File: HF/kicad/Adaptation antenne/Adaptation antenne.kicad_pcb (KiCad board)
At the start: 2 copper layers, 40.8 x 23.7 mm, 6 parts, among them J1 Conn_Coaxial, J2 Impédence Antenne, J3 impédence GND, J4 Sortie vers antenne, J5 Sortie vers GND, J6 Antenne

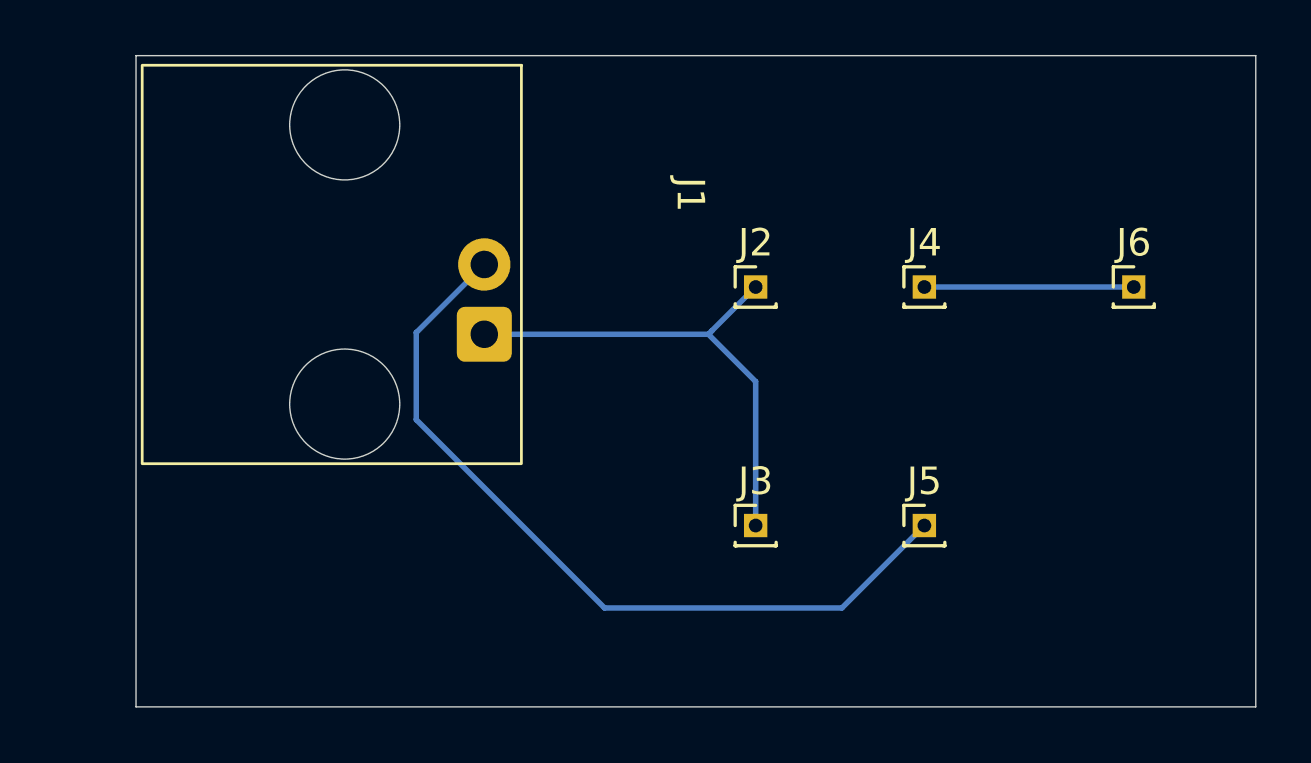
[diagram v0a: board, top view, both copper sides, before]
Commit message: modif kicad pour ajusté au test sur platin
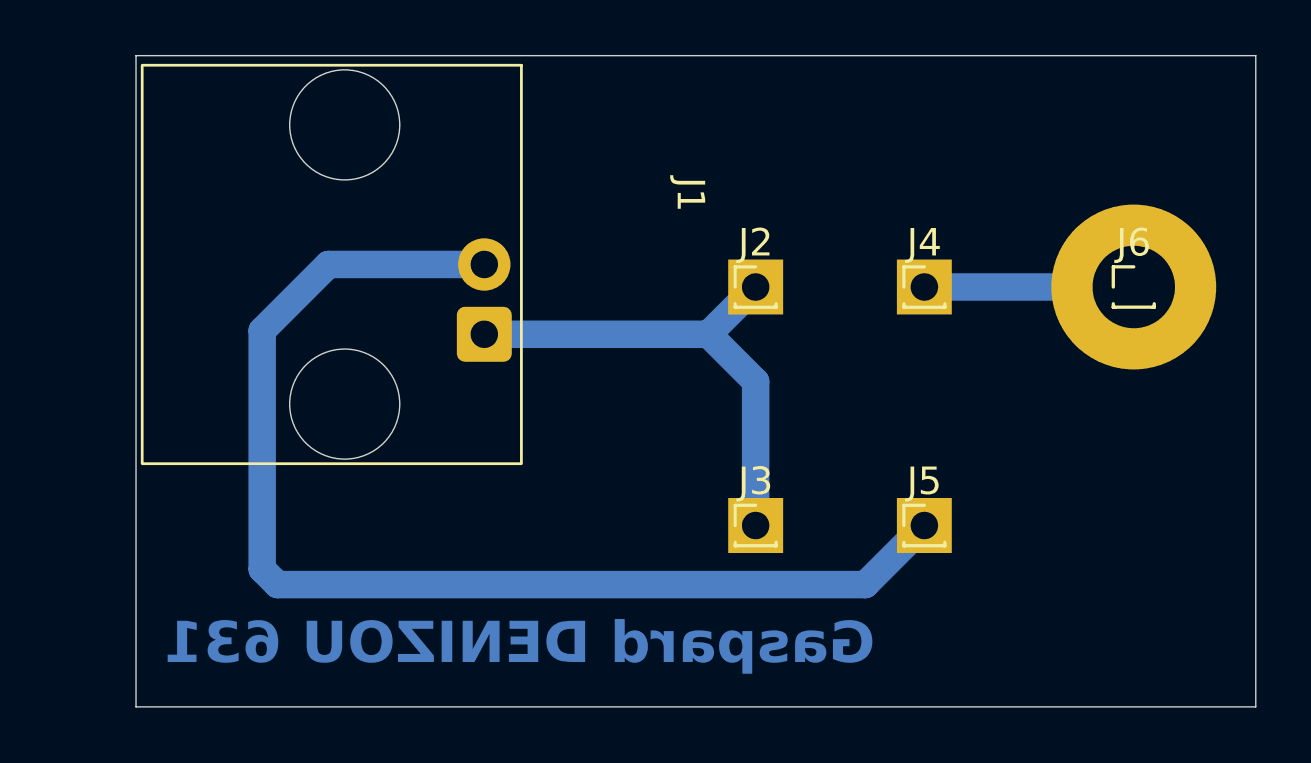
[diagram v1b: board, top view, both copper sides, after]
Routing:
- net GND: track 29.2 -> 43.0 mm
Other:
- board text added: "Gaspard DENIZOU 631"
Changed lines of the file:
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@@
 		(tenting front back)
 		(pcbplotparams
-			(layerselection 0x00000000_00000000_55555555_5755f5ff)
+			(layerselection 0x00000000_00000000_55555555_57555555)
 			(plot_on_all_layers_selection 0x00000000_00000000_00000000_00000000)
 			(disableapertmacros no)
@@
 			(outputformat 1)
 			(mirror no)
-			(drillshape 1)
+			(drillshape 0)
 			(scaleselection 1)
 			(outputdirectory "")
@@
 		(pad "1" thru_hole rect
 			(at 0 0)
-			(size 0.85 0.85)
-			(drill 0.5)
+			(size 2 2)
+			(drill 1)
 			(layers "*.Cu" "*.Mask")
 			(remove_unused_layers no)
@@
 		(pad "1" thru_hole rect
 			(at 0 0)
-			(size 0.85 0.85)
-			(drill 0.5)
+			(size 2 2)
+			(drill 1)
 			(layers "*.Cu" "*.Mask")
 			(remove_unused_layers no)
@@
 		(pad "1" thru_hole rect
 			(at 0 0)
-			(size 0.85 0.85)
-			(drill 0.5)
+			(size 2 2)
+			(drill 1)
 			(layers "*.Cu" "*.Mask")
 			(remove_unused_layers no)
@@
 			)
 		)
-		(pad "1" thru_hole rect
+		(pad "1" thru_hole circle
 			(at 0 0)
-			(size 0.85 0.85)
-			(drill 0.5)
+			(size 6 6)
+			(drill 3)
 			(layers "*.Cu" "*.Mask")
 			(remove_unused_layers no)
@@
 		(pad "1" thru_hole rect
 			(at 0 0)
-			(size 0.85 0.85)
-			(drill 0.5)
+			(size 2 2)
+			(drill 1)
 			(layers "*.Cu" "*.Mask")
 			(remove_unused_layers no)
@@
 		(layer "F.Fab")
 	)
+	(gr_text "Gaspard DENIZOU 631"
+		(at 38.85 34.15 0)
+		(layer "B.Cu")
+		(effects
+			(font
+				(size 1.5 1.5)
+				(thickness 0.3)
+				(bold yes)
+			)
+			(justify left bottom mirror)
+		)
+	)
 	(segment
 		(start 34.5 23.76)
 		(end 32.78 22.04)
-		(width 0.2)
+		(width 1)
 		(layer "B.Cu")
 		(net 1)
@@
 		(start 34.5 29)
 		(end 34.5 23.76)
-		(width 0.2)
+		(width 1)
 		(layer "B.Cu")
 		(net 1)
@@
 		(start 32.78 22.04)
 		(end 32.91 21.91)
-		(width 0.2)
+		(width 1)
 		(layer "B.Cu")
 		(net 1)
@@
 		(start 32.91 21.91)
 		(end 34.5 20.32)
-		(width 0.2)
+		(width 1)
 		(layer "B.Cu")
 		(net 1)
@@
 		(start 24.625 22.04)
 		(end 32.78 22.04)
-		(width 0.2)
+		(width 1)
 		(layer "B.Cu")
 		(net 1)
 	)
 	(segment
-		(start 29 32)
-		(end 37.64 32)
-		(width 0.2)
+		(start 16.541502 30.591502)
+		(end 16.541502 21.908498)
+		(width 1)
 		(layer "B.Cu")
 		(net 2)
 	)
 	(segment
-		(start 37.64 32)
-		(end 40.64 29)
-		(width 0.2)
+		(start 17.1 31.15)
+		(end 16.541502 30.591502)
+		(width 1)
 		(layer "B.Cu")
 		(net 2)
 	)
 	(segment
-		(start 22.148498 25.148498)
-		(end 29 32)
-		(width 0.2)
+		(start 16.541502 21.908498)
+		(end 18.95 19.5)
+		(width 1)
 		(layer "B.Cu")
 		(net 2)
 	)
 	(segment
-		(start 22.148498 21.976502)
-		(end 22.148498 25.148498)
-		(width 0.2)
+		(start 40.64 29)
+		(end 38.49 31.15)
+		(width 1)
 		(layer "B.Cu")
 		(net 2)
 	)
 	(segment
-		(start 24.625 19.5)
-		(end 22.148498 21.976502)
-		(width 0.2)
+		(start 18.95 19.5)
+		(end 24.625 19.5)
+		(width 1)
+		(layer "B.Cu")
+		(net 2)
+	)
+	(segment
+		(start 38.49 31.15)
+		(end 17.1 31.15)
+		(width 1)
 		(layer "B.Cu")
 		(net 2)
@@
 		(start 48.26 20.32)
 		(end 40.64 20.32)
-		(width 0.2)
+		(width 1)
 		(layer "B.Cu")
 		(net 3)
